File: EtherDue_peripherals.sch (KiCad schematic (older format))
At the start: 5 parts, among them U701 MICROSD, U702 24AA025E48

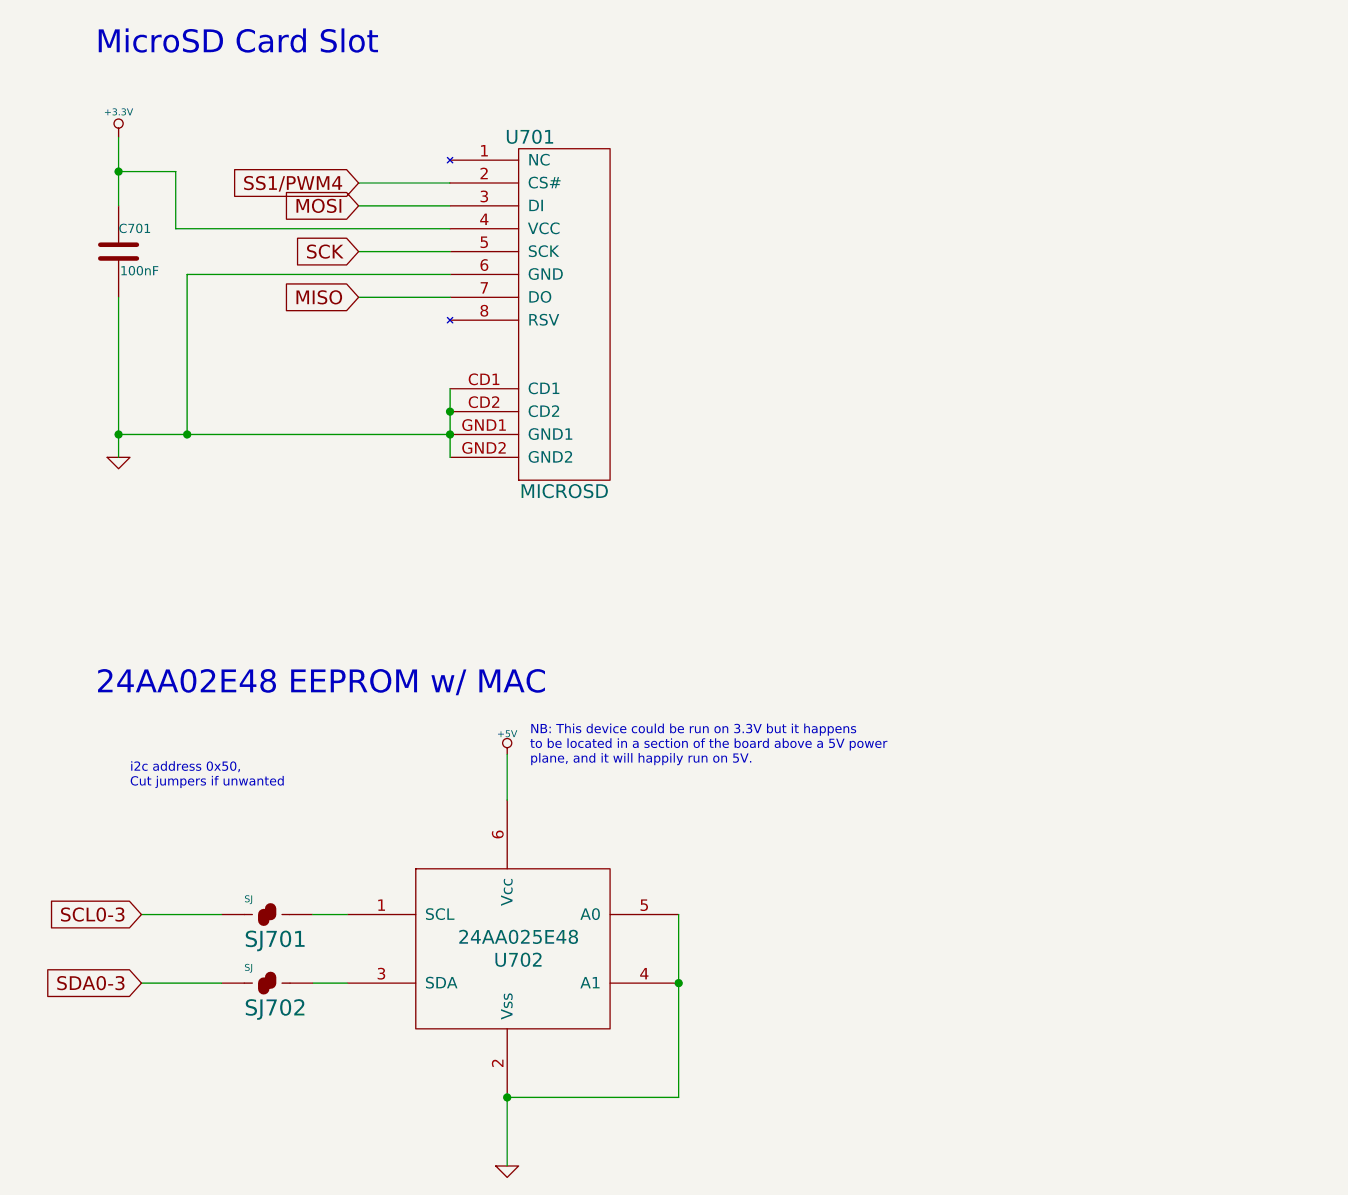
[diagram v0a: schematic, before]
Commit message: Update EtherDue from Kicad 2013-07 to 2014-07 (incl. "pretty" footprints, etc.)
New netlist has been imported into PCB but new "pretty" footprint
associations HAVE NOT, need to take care if replacing any of these
from the new libraries as associations may be different.
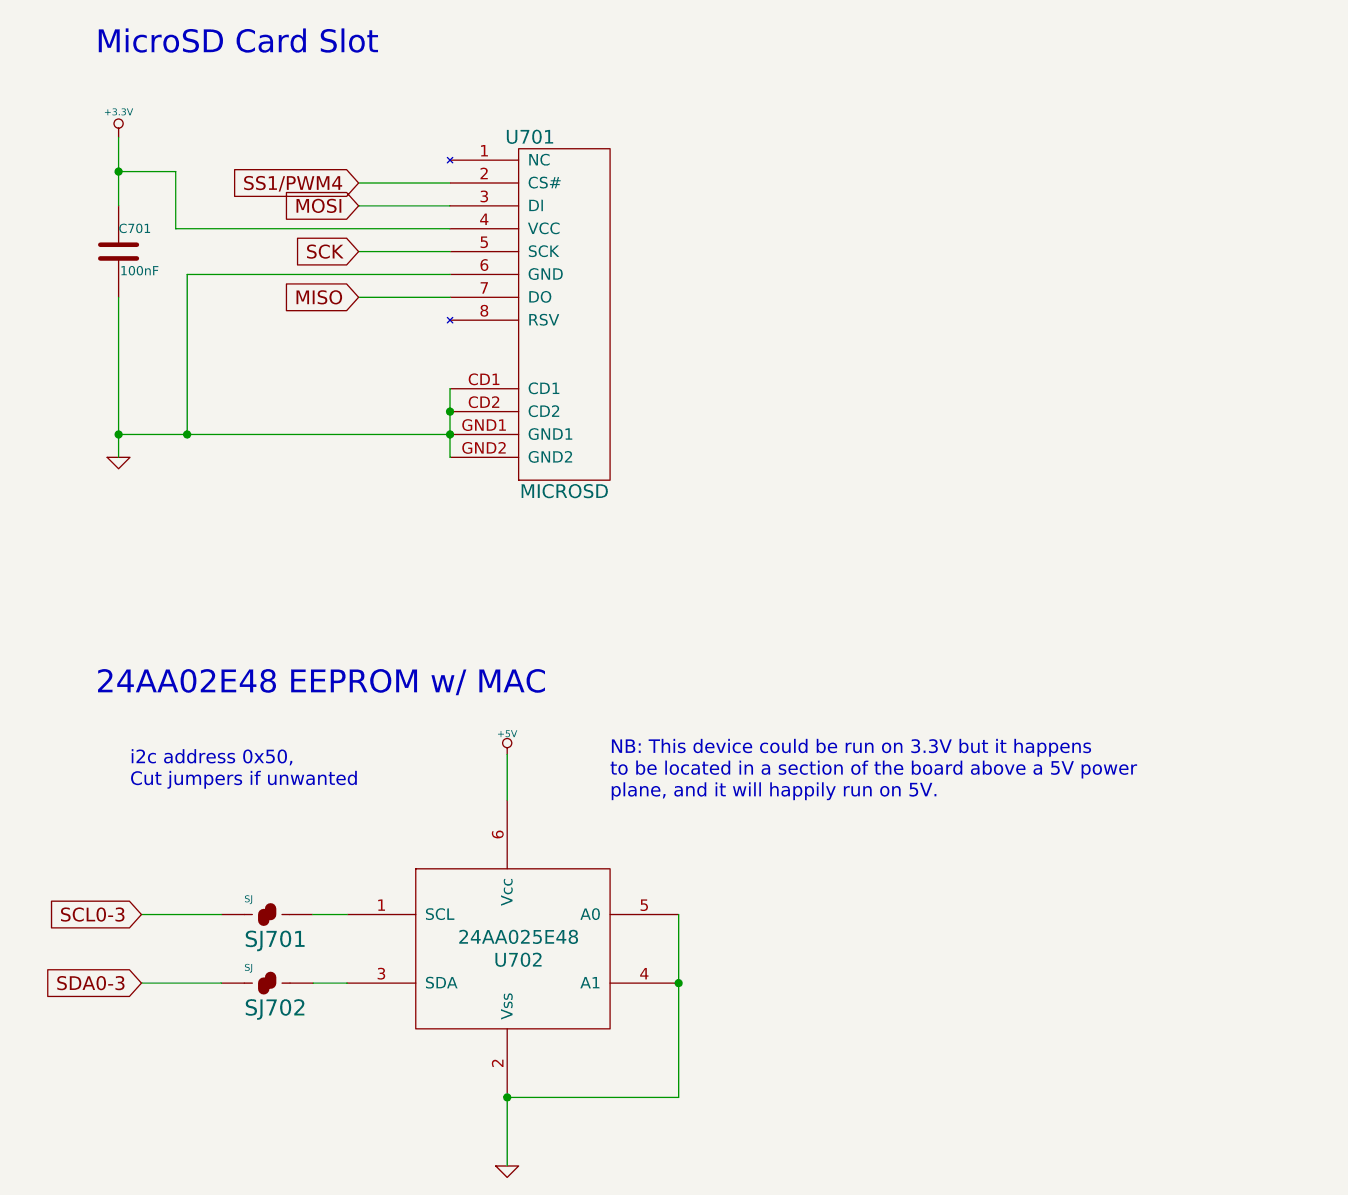
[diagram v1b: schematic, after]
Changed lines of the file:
@@
 LIBS:valves
 LIBS:EtherDue-cache
-EELAYER 27 0
+EELAYER 24 0
 EELAYER END
 $Descr A4 11693 8268
 encoding utf-8
-Sheet 7 7
+Sheet 6 7
 Title "EtherDue"
 Date "16 jan 2014"
@@
 Connection ~ 3850 5100
 Connection ~ 3100 5600
-Text Notes 1450 4250 0    40   ~ 0
+Text Notes 1450 4250 0    59   ~ 0
 i2c address 0x50,\nCut jumpers if unwanted
 Text Notes 1300 1050 0    100  ~ 0
@@
 	1    0    0    -1
 $EndComp
-Text Notes 3200 4150 0    40   ~ 0
+Text Notes 3550 4300 0    59   ~ 0
 NB: This device could be run on 3.3V but it happens\nto be located in a section of the board above a 5V power\nplane, and it will happily run on 5V.
 $EndSCHEMATC
